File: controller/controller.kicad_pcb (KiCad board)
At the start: 2 copper layers, 160 x 100 mm, 14 parts, among them J2 Barrel_Jack_Switch, J3 Conn_01x02, P1 PMOD-Device-x2-Type-Generic-A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, P2 PMOD-Device-x2-Type-Generic-A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, P3 PMOD-Device-x2-Type-Generic-A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, U1 MAX4820xUP, U2 USB3300-EZK, U3 NUCLEO144-F767ZI, U4 TSR_1-2450

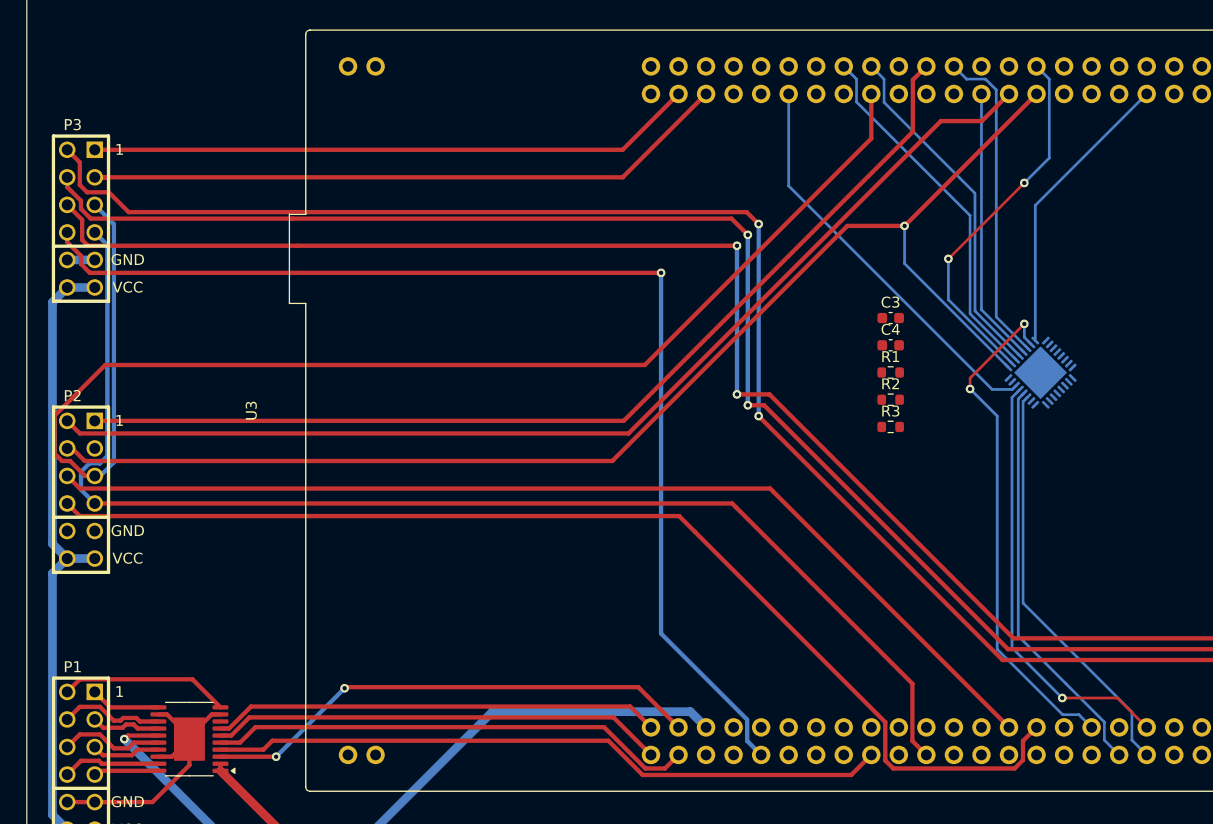
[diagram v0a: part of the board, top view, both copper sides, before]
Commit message: remove USB HS PHY
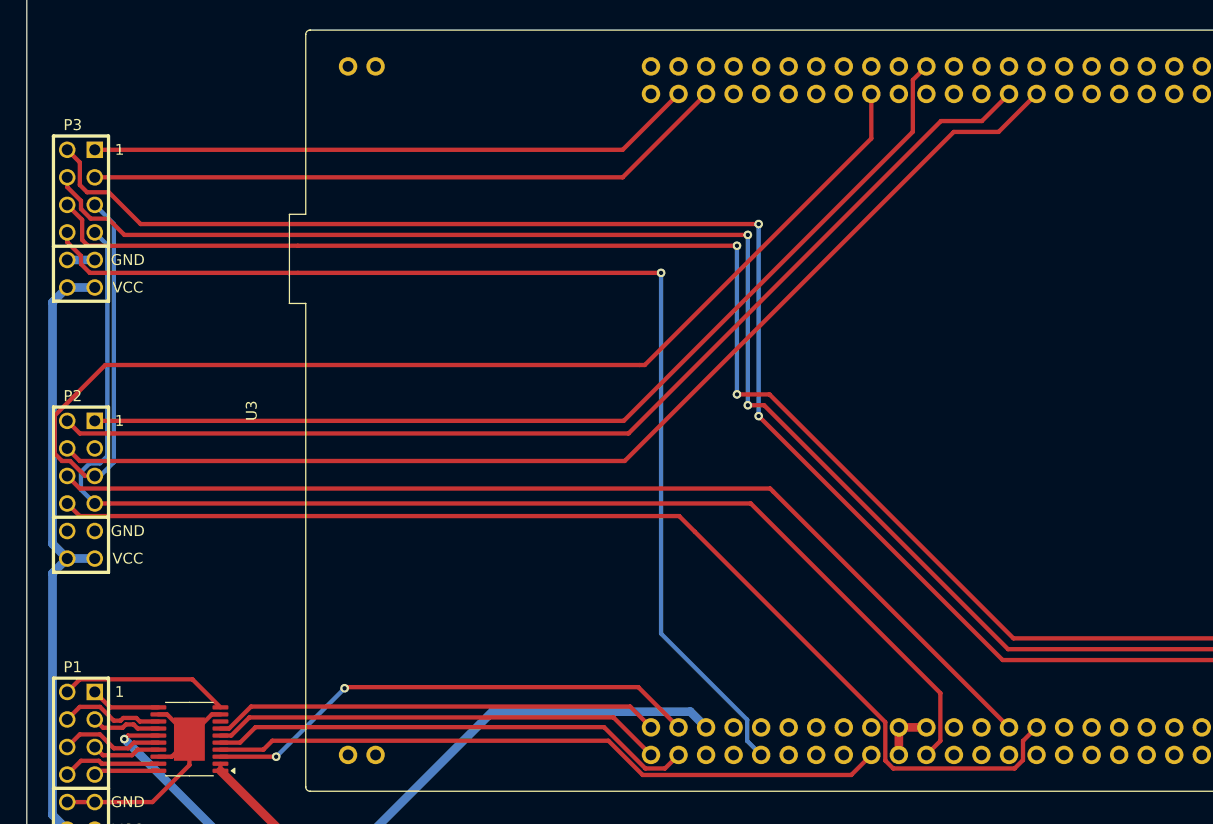
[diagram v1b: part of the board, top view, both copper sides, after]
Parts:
- removed C3, C4: C, Capacitor_SMD:C_0603_1608Metric
- removed R1: 12 kR 1%, Resistor_SMD:R_0603_1608Metric
- removed R2, R3: R, Resistor_SMD:R_0603_1608Metric
- removed U2: USB3300-EZK, Package_DFN_QFN:QFN-32-1EP_5x5mm_P0.5mm_EP3.45x3.45mm
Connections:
- U3 pad 102: ULPI_D6 -> unconnected-(U3-ETH_TXD1/PB13-Pad102)
- U3 pad 109: ULPI_D0 -> unconnected-(U3-PA3-Pad109)
- U3 pad 34: ULPI_D1 -> unconnected-(U3-PB0-Pad34)
- U3 pad 35: ULPI_DIR -> unconnected-(U3-PC2-Pad35)
- U3 pad 37: ULPI_NXT -> unconnected-(U3-PC3-Pad37)
- U3 pad 38: ULPI_STP -> unconnected-(U3-PC0-Pad38)
- U3 pad 83: ULPI_CLKOUT -> unconnected-(U3-PA5-Pad83)
- U3 pad 88: ULPI_D5 -> unconnected-(U3-PB12-Pad88)
- U3 pad 90: ULPI_D4 -> unconnected-(U3-PB11-Pad90)
- U3 pad 96: ULPI_D2 -> unconnected-(U3-PB1-Pad96)
- U3 pad 97: ULPI_D3 -> unconnected-(U3-PB10-Pad97)
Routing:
- net ULPI_D1: track 47.0 -> 0.00 mm, vias 2 -> 0
- net ULPI_STP: track 39.6 -> 0.00 mm, vias 1 -> 0
- net ULPI_NXT: track 37.9 -> 0.00 mm
- net ULPI_DIR: track 37.4 -> 0.00 mm
- net ULPI_CLKOUT: track 37.4 -> 0.00 mm
- net ULPI_D6: track 34.2 -> 0.00 mm, vias 2 -> 0
- net ULPI_D5: track 33.6 -> 0.00 mm
- net ULPI_D4: track 32.4 -> 0.00 mm
- net ULPI_D2: track 29.8 -> 0.00 mm
- net ULPI_D0: track 27.0 -> 0.00 mm
- net ULPI_D3: track 25.4 -> 0.00 mm
- net TX_Q: track 120.9 -> 103.9 mm, vias 1 -> 0
- net GND: track 46.5 -> 51.5 mm
- net SDA: track 117.0 -> 119.0 mm
- net UI1: track 60.6 -> 59.6 mm

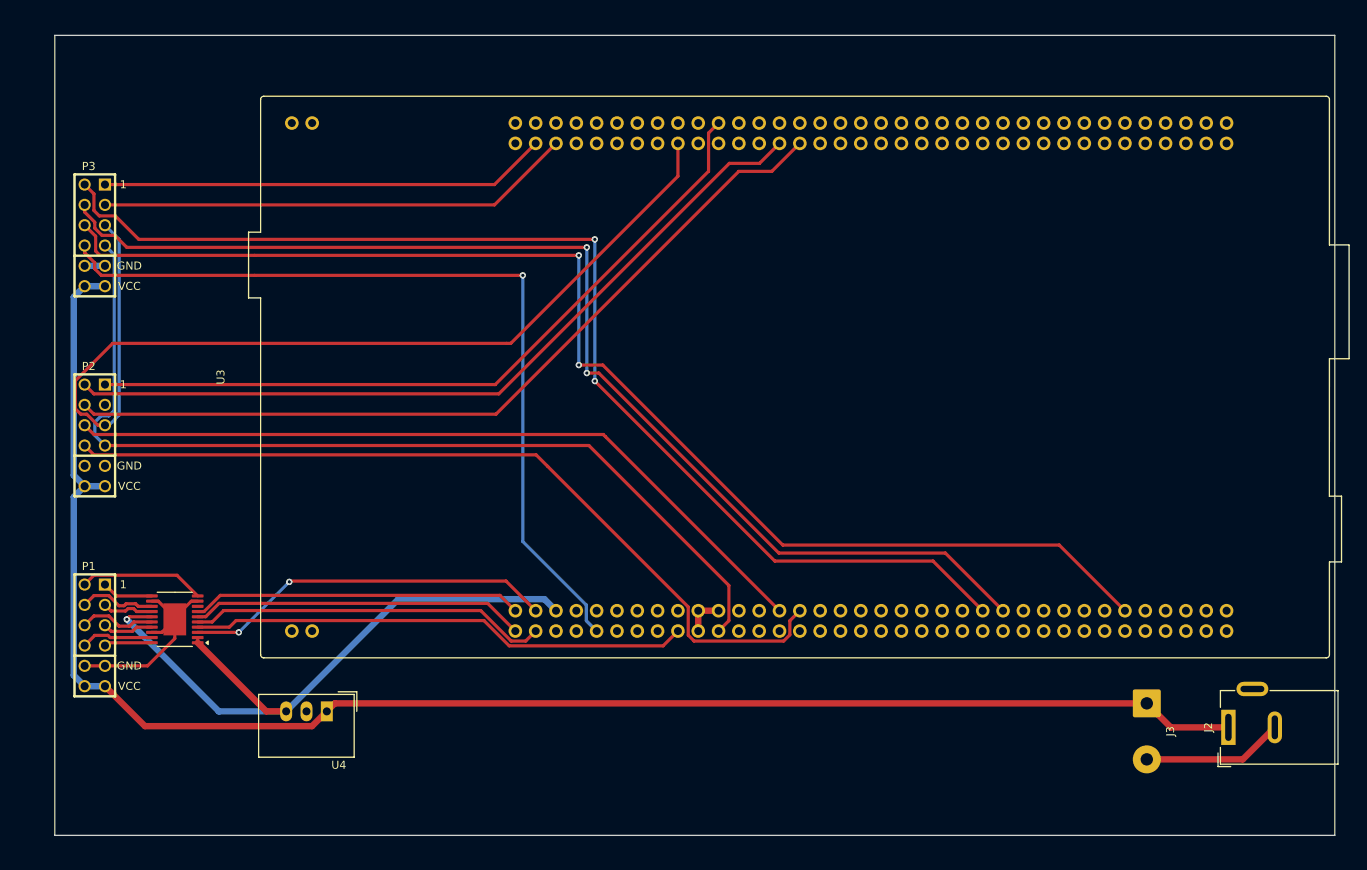
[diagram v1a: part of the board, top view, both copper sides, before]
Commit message: replace RF connectors, add missing silkscreen text
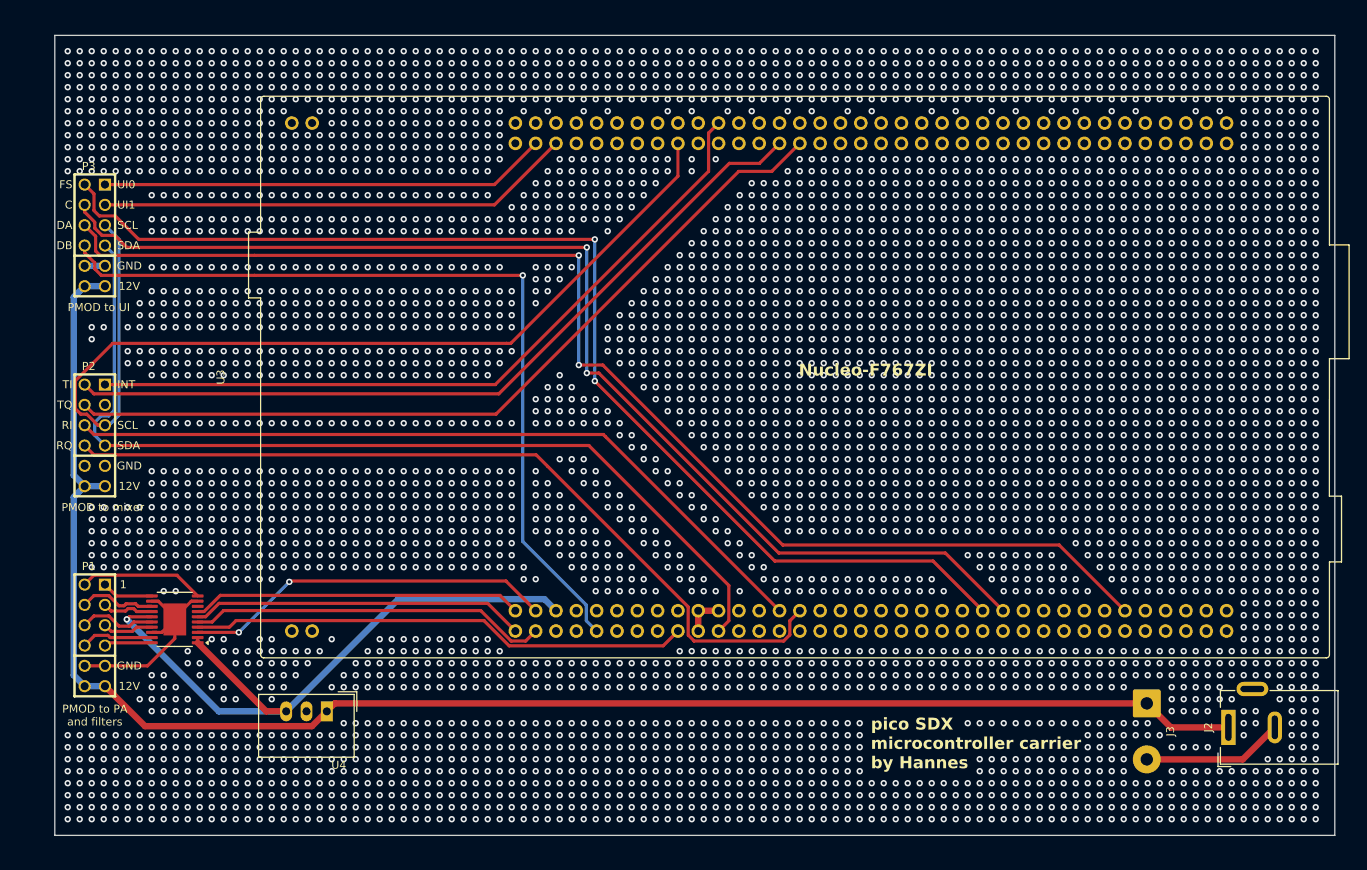
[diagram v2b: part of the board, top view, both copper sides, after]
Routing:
- net GND: vias 0 -> 4790
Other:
- board text added: "C"
- board text added: "DA"
- board text added: "DB"
- board text added: "FS"
- board text added: "INT"
- board text added: "Nucleo-F767ZI"
- board text added: "PMOD to PA and filters"
- board text added: "PMOD to UI"
- board text added: "PMOD to mixer"
- board text added: "RI"
- board text added: "RQ"
- board text added: "SCL"
- board text added: "SDA"
- board text added: "TI"
- board text added: "TQ"
- board text added: "UI0"
- board text added: "UI1"
- board text added: "pico SDX microcontroller carrier by Hannes"

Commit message: clean up
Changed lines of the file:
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@@
 			(at -1.5 -6.71 0)
 			(layer "F.SilkS")
+			(hide yes)
 			(effects
 				(font
@@
 			(at -0.762 -8.636 0)
 			(layer "F.SilkS")
+			(hide yes)
 			(effects
 				(font
@@
 			(at 3.5 -2.95 90)
 			(layer "F.SilkS")
+			(hide yes)
 			(effects
 				(font
@@
 			(at -0.762 -8.636 0)
 			(layer "F.SilkS")
+			(hide yes)
 			(effects
 				(font
@@
 			(at 0 -2.5 90)
 			(layer "F.SilkS")
+			(hide yes)
 			(effects
 				(font
@@
 			(at -0.762 -8.636 0)
 			(layer "F.SilkS")
+			(hide yes)
 			(effects
 				(font
@@
 			(at 31.75 -36.83 90)
 			(layer "F.SilkS")
+			(hide yes)
 			(effects
 				(font
@@
 		)
 		(height -8)
-		(gr_text "984.2520 mils"
+		(gr_text "25.0000 mm"
 			(at 5.935 42.186 90)
 			(layer "Dwgs.User")
@@
 		)
 		(height -8)
-		(gr_text "984.2520 mils"
+		(gr_text "25.0000 mm"
 			(at 5.935 67.186 90)
 			(layer "Dwgs.User")
@@
 		)
 		(height -8)
-		(gr_text "492.1260 mils"
+		(gr_text "12.5000 mm"
 			(at 5.935 23.436 90)
 			(layer "Dwgs.User")
@@
 		)
 		(height -8)
-		(gr_text "492.1260 mils"
+		(gr_text "12.5000 mm"
 			(at 5.935 98.436 90)
 			(layer "Dwgs.User")
@@
 		)
 		(height -16.5)
-		(gr_text "492.1260 mils"
+		(gr_text "12.5000 mm"
 			(at -2.565 110.936 90)
 			(layer "Dwgs.User")
@@
 		)
 		(height -16.5)
-		(gr_text "984.2520 mils"
+		(gr_text "25.0000 mm"
 			(at -2.565 92.186 90)
 			(layer "Dwgs.User")

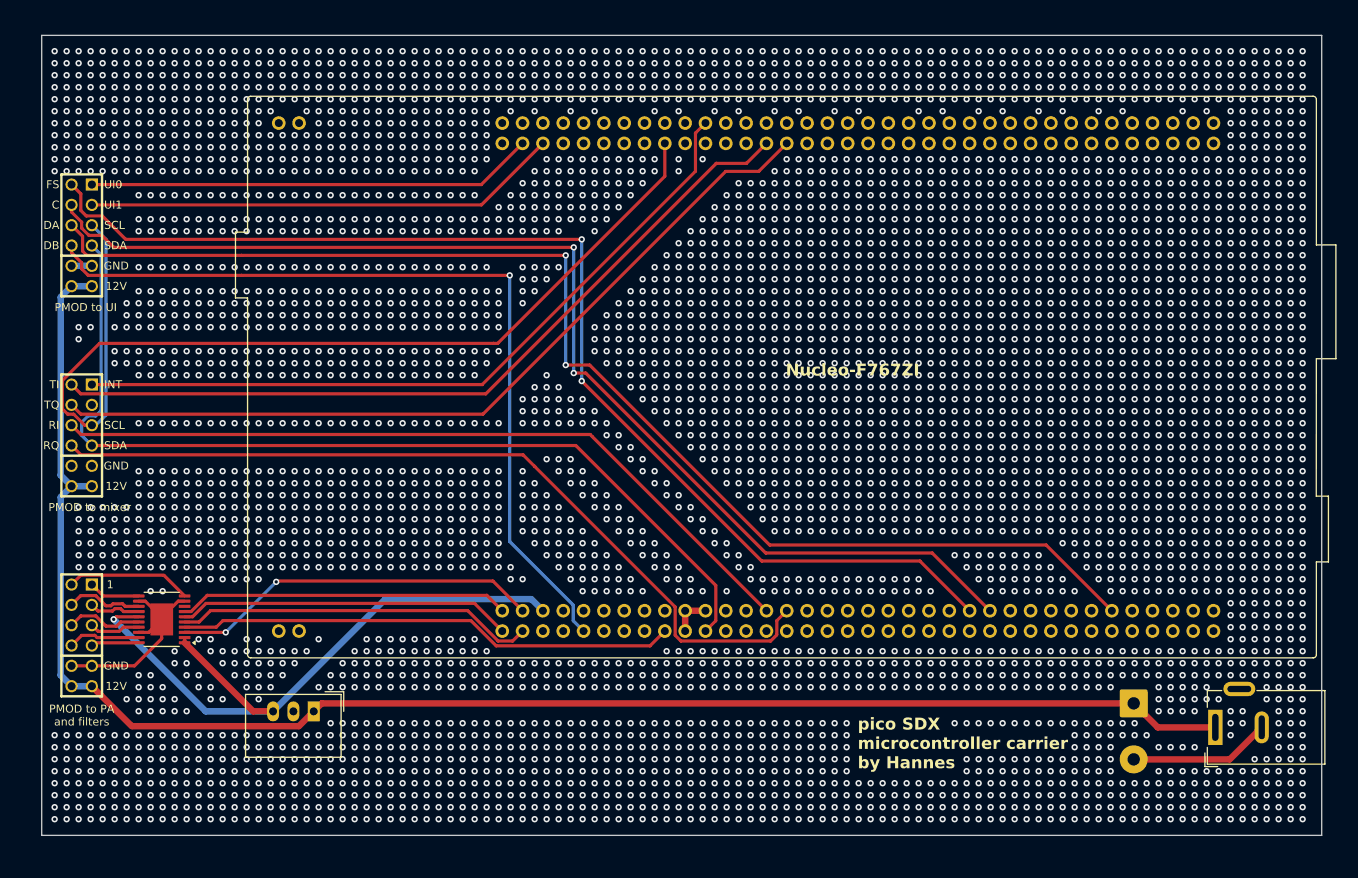
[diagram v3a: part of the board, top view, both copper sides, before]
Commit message: use ZIO footprint for Nucleo
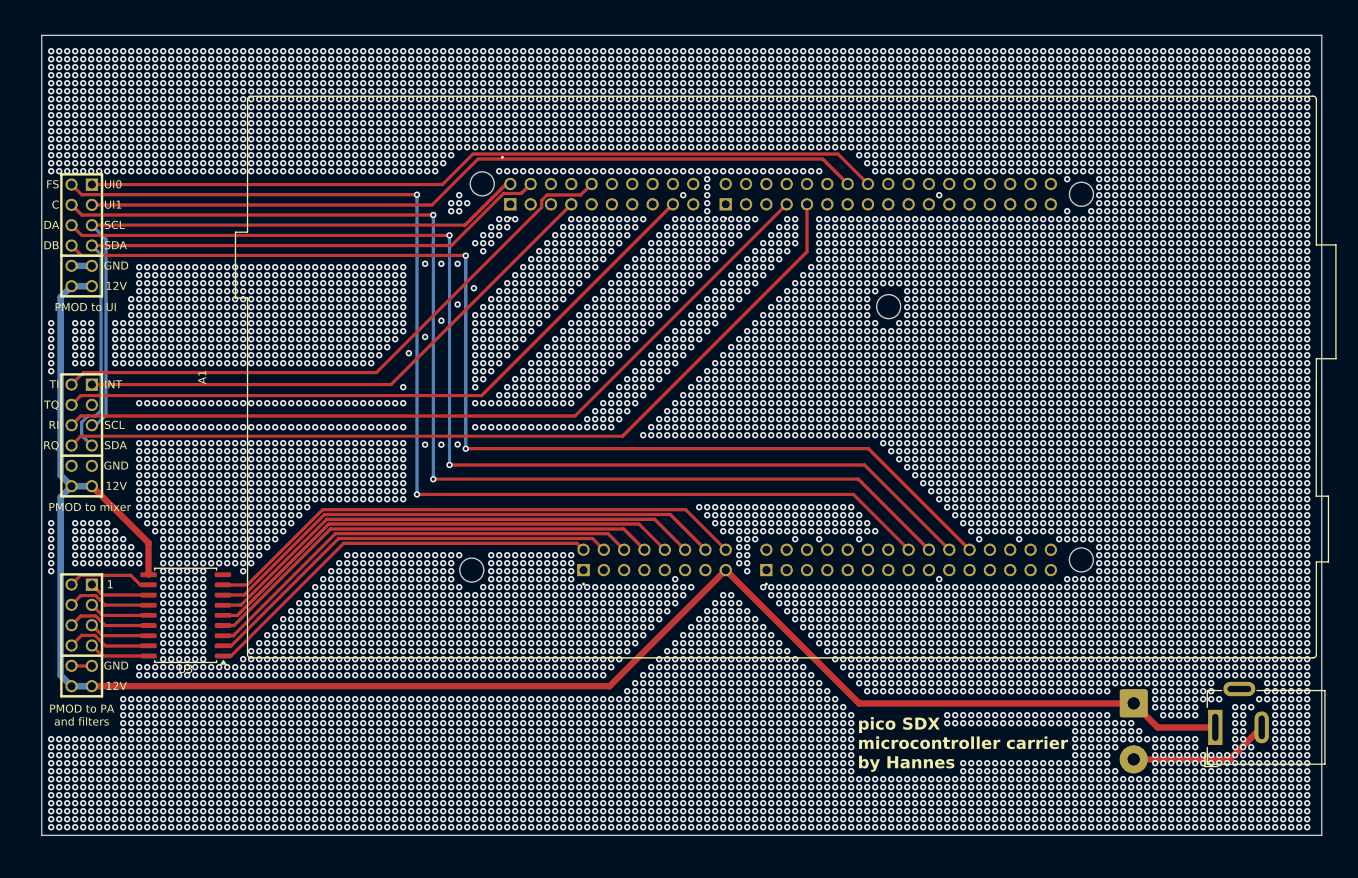
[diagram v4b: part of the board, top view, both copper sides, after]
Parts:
- removed U1: MAX4820xUP, Package_SO:HTSSOP-20-1EP_4.4x6.5mm_P0.65mm_EP2.85x4mm
- removed U4: TSR_1-2450, Converter_DCDC:Converter_DCDC_TRACO_TSR-1_THT
- added A1: NUCLEO144-H767ZI, crossover:ST_Zio_Connectors_144_STLink, F.Cu at (73.3, 91.6)
- U3: value NUCLEO144-F767ZI -> ULN2803A; footprint Module:ST_Morpho_Connector_144_STLink -> Package_SO:SOIC-18W_7.5x11.6mm_P1.27mm
- moved U3 39.6 mm to (33.7, 89.7), turned to 180 degrees
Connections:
- U3 pad 1: SCLK -> Net-(A1A-D43/PC8/SDMMC_D0)
- U3 pad 10: unconnected-(U3-NC-Pad10) -> +12V
- U3 pad 11: SAI_MCLK_B -> TX~{RX}
- U3 pad 12: unconnected-(U3-IOREF-Pad12) -> 10 m
- U3 pad 13: unconnected-(U3-TMS/PA13-Pad13) -> 12 m
- U3 pad 14: unconnected-(U3-~{RST}-Pad14) -> 15 m
- U3 pad 15: unconnected-(U3-TCK/PA14-Pad15) -> 17 m
- U3 pad 16: +3.3V -> 20 m
- U3 pad 17: ~{CS} -> 30 m
- U3 pad 18: unconnected-(U3-+5V-Pad18) -> 40 m
- U3 pad 2: MISO -> Net-(A1A-D44/PC9/SDMMC_D1/I2S_B_CKIN)
- U3 pad 3: MOSI -> Net-(A1A-D45/PC10/SDMMC_D2)
- U3 pad 4: ~{RESET} -> Net-(A1A-D46/PC11/SDMMC_D3)
- U3 pad 5: unconnected-(U3-VDD-Pad5) -> Net-(A1A-D47/PC12/SDMMC_CK)
- U3 pad 6: +5VD -> Net-(A1A-D48/PD2/SDMMC_CMD)
- U3 pad 7: unconnected-(U3-~{BOOT0}-Pad7) -> Net-(A1A-D49/PG2/IO)
- U3 pad 8: GND -> Net-(A1A-D50/PG3/IO)
- U3 pad 9: SAI_SD_B -> GND
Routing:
- net +5VD: track 83.4 -> 0.00 mm, vias 1 -> 0
- net Net-(A1A-D50/PG3/IO): track 0.00 -> 68.8 mm
- net Net-(A1A-D49/PG2/IO): track 0.00 -> 66.3 mm
- net Net-(A1A-D48/PD2/SDMMC_CMD): track 0.00 -> 63.8 mm
- net ~{CS}: track 62.4 -> 0.00 mm
- net Net-(A1A-D47/PC12/SDMMC_CK): track 0.00 -> 61.3 mm
- net Net-(A1A-D46/PC11/SDMMC_D3): track 0.00 -> 58.8 mm
- net Net-(A1A-D45/PC10/SDMMC_D2): track 0.00 -> 56.3 mm
- net Net-(A1A-D44/PC9/SDMMC_D1/I2S_B_CKIN): track 0.00 -> 53.8 mm
- net Net-(A1A-D43/PC8/SDMMC_D0): track 0.00 -> 51.2 mm
- net ~{RESET}: track 46.4 -> 0.00 mm, vias 2 -> 0
- net MOSI: track 44.9 -> 0.00 mm
- net UI0: track 56.0 -> 100.1 mm
- net SCL: track 124.8 -> 81.2 mm
- net SCLK: track 41.8 -> 0.00 mm
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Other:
- board text removed: "Nucleo-F767ZI"
